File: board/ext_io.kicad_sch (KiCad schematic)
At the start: 34 parts, among them J10 CAN_2, J6 AIN, J7 CAN_1, J8 DIO1, J9 DIO0, SW16 Term, SW17 Term, U13 25LCxxx, U14 MCP2515-xP, U15 MCP3204, U16 MCP2562-E-P, U17 MCP2515-xP, U18 MCP23S17_SP, U19 MCP2562-E-P, Y2 16MHz, Y3 16MHz

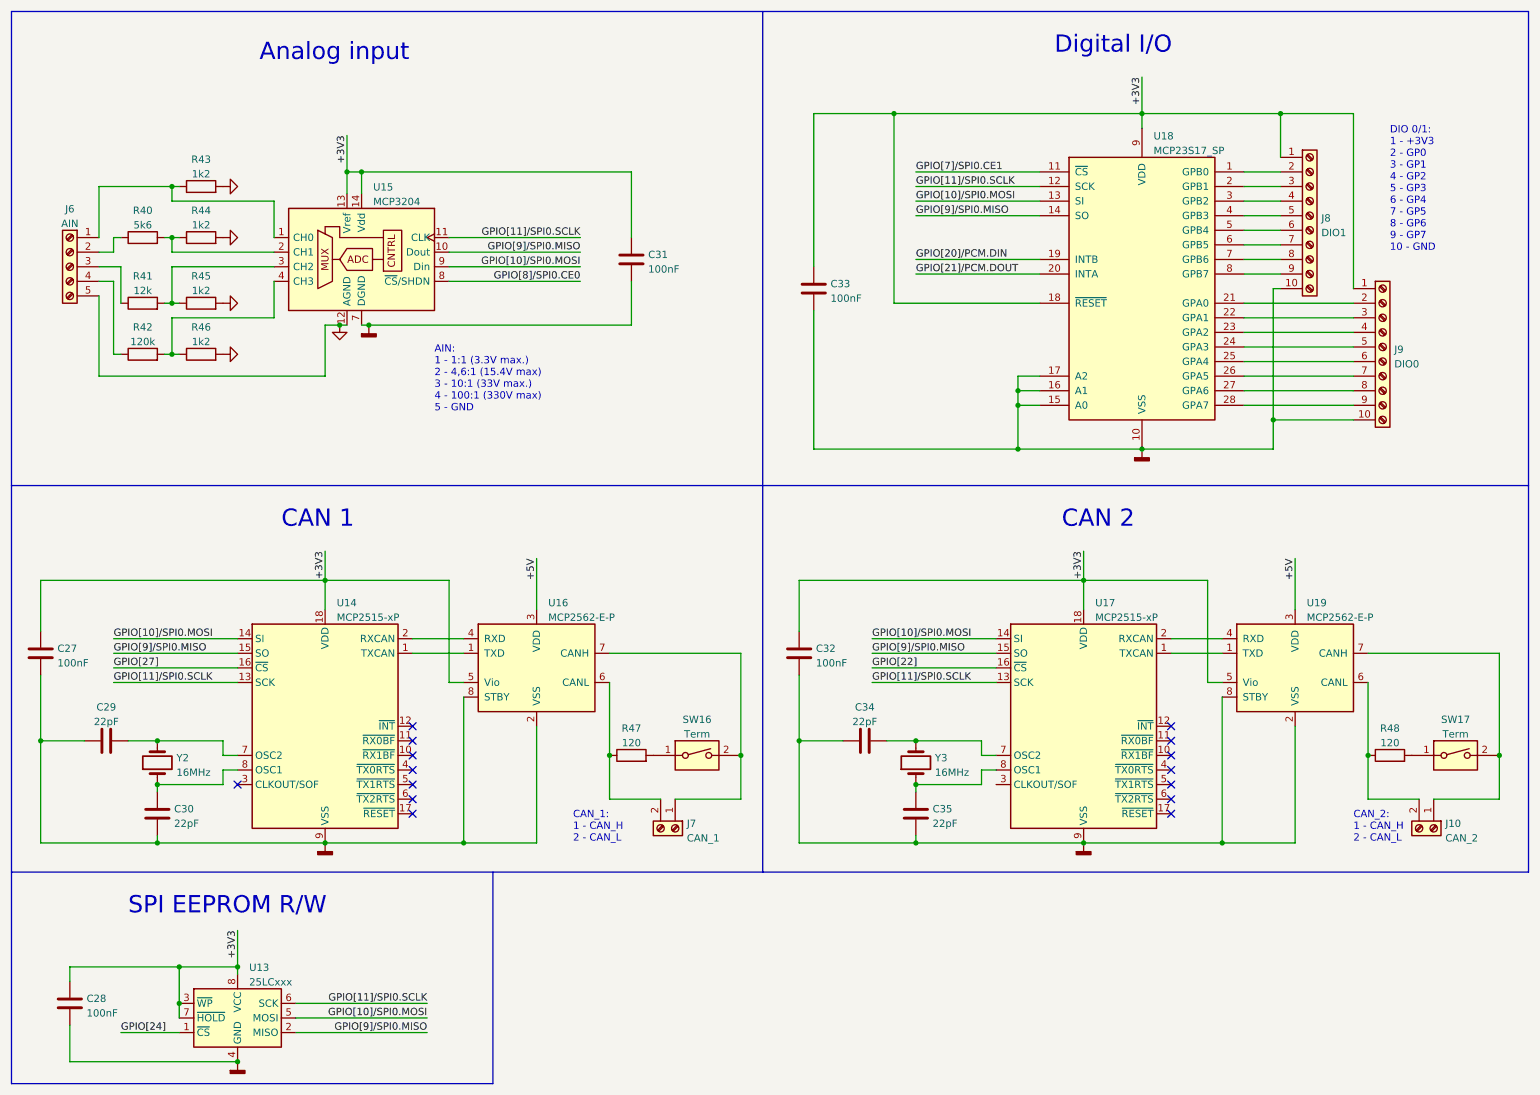
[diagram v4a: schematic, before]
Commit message: Add missing footprints.
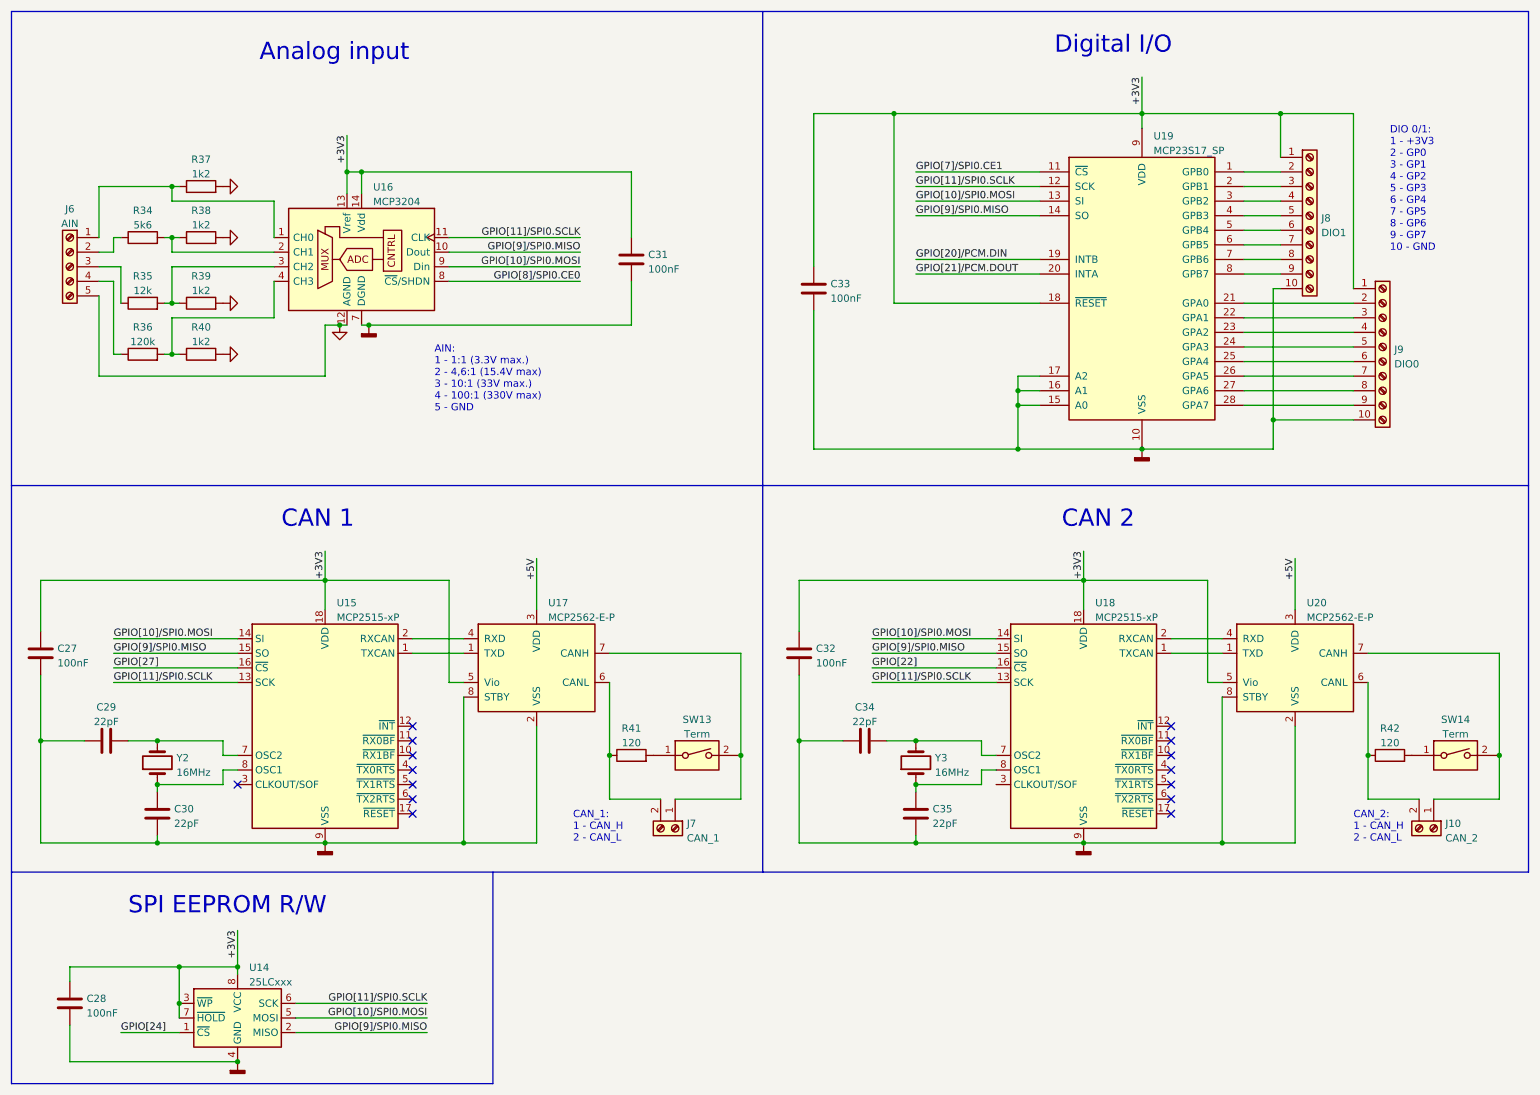
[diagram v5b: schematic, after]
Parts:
- C27, C28, C31, C32, C33, C34, C35: footprint (none) -> Capacitor_THT:C_Disc_D5.0mm_W2.5mm_P5.00mm
- C29, C30: footprint (none) -> Capacitor_THT:C_Radial_D6.3mm_H5.0mm_P2.50mm
- J10, J7: footprint (none) -> TerminalBlock_TE-Connectivity:TerminalBlock_TE_282834-2_1x02_P2.54mm_Horizontal
- J6: footprint (none) -> TerminalBlock_TE-Connectivity:TerminalBlock_TE_282834-5_1x05_P2.54mm_Horizontal
- J8, J9: footprint (none) -> TerminalBlock_TE-Connectivity:TerminalBlock_TE_1-282834-0_1x10_P2.54mm_Horizontal
- R34: renamed from R40; footprint (none) -> Resistor_THT:R_Axial_DIN0516_L15.5mm_D5.0mm_P7.62mm_Vertical
- R35: renamed from R41; footprint (none) -> Resistor_THT:R_Axial_DIN0516_L15.5mm_D5.0mm_P7.62mm_Vertical
- R36: renamed from R42; footprint (none) -> Resistor_THT:R_Axial_DIN0516_L15.5mm_D5.0mm_P7.62mm_Vertical
- R37: renamed from R43; footprint (none) -> Resistor_THT:R_Axial_DIN0516_L15.5mm_D5.0mm_P7.62mm_Vertical
- R38: renamed from R44; footprint (none) -> Resistor_THT:R_Axial_DIN0516_L15.5mm_D5.0mm_P7.62mm_Vertical
- R39: renamed from R45; footprint (none) -> Resistor_THT:R_Axial_DIN0516_L15.5mm_D5.0mm_P7.62mm_Vertical
- R40: renamed from R46; footprint (none) -> Resistor_THT:R_Axial_DIN0516_L15.5mm_D5.0mm_P7.62mm_Vertical
- R41: renamed from R47; footprint (none) -> Resistor_THT:R_Axial_DIN0516_L15.5mm_D5.0mm_P7.62mm_Vertical
- R42: renamed from R48; footprint (none) -> Resistor_THT:R_Axial_DIN0516_L15.5mm_D5.0mm_P7.62mm_Vertical
- SW13: renamed from SW16; footprint (none) -> Button_Switch_THT:SW_DIP_SPSTx01_Slide_6.7x4.1mm_W7.62mm_P2.54mm_LowProfile
- SW14: renamed from SW17; footprint (none) -> Button_Switch_THT:SW_DIP_SPSTx01_Slide_6.7x4.1mm_W7.62mm_P2.54mm_LowProfile
- U16: renamed from U15; footprint (none) -> Package_DIP:DIP-12_W7.62mm_Socket_LongPads
- Y2, Y3: footprint (none) -> Crystal:Crystal_HC49-U_Vertical
- renumbered U13 to U14, U14 to U15, U16 to U17, U17 to U18, U18 to U19, U19 to U20

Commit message: Change net descriptors.
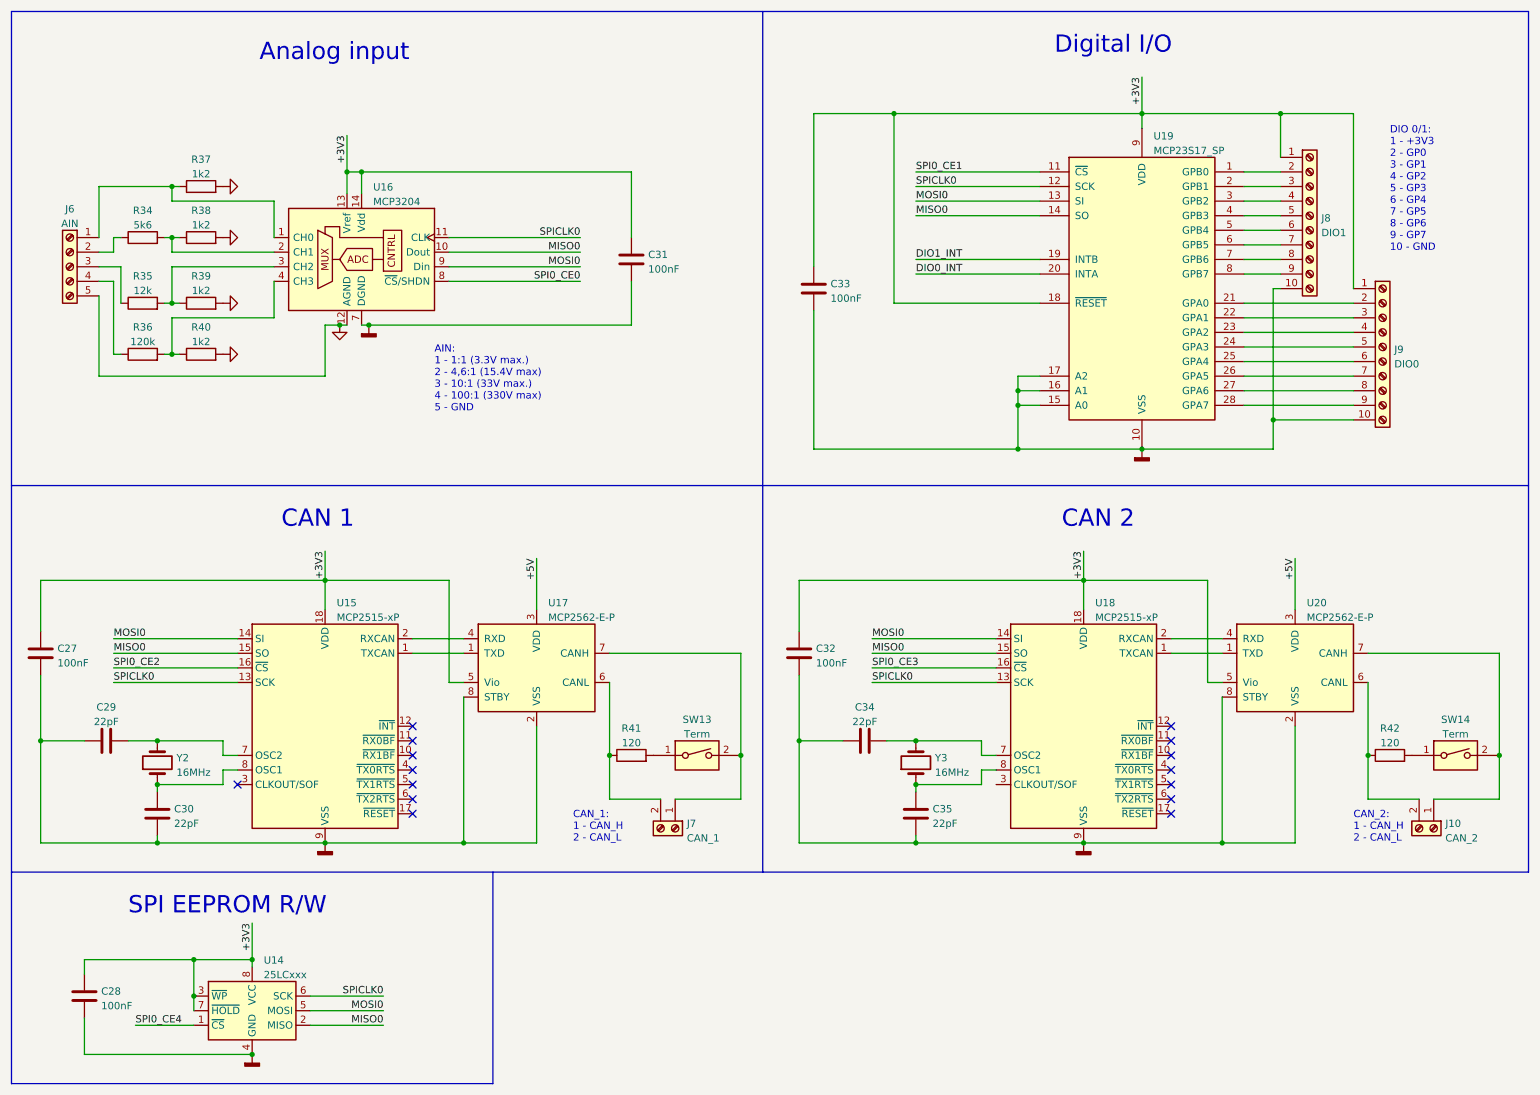
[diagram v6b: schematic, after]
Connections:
- net GPIO[10]/SPI0.MOSI renamed MOSI0
- net GPIO[11]/SPI0.SCLK renamed SPICLK0
- net GPIO[20]/PCM.DIN renamed DIO1_INT
- net GPIO[21]/PCM.DOUT renamed DIO0_INT
- net GPIO[22] renamed SPI0_CE3
- net GPIO[24] renamed SPI0_CE4
- net GPIO[27] renamed SPI0_CE2
- net GPIO[7]/SPI0.CE1 renamed SPI0_CE1
- net GPIO[8]/SPI0.CE0 renamed SPI0_CE0
- net GPIO[9]/SPI0.MISO renamed MISO0
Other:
- moved on the sheet: C28, U14

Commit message: Make it a multiboard project.
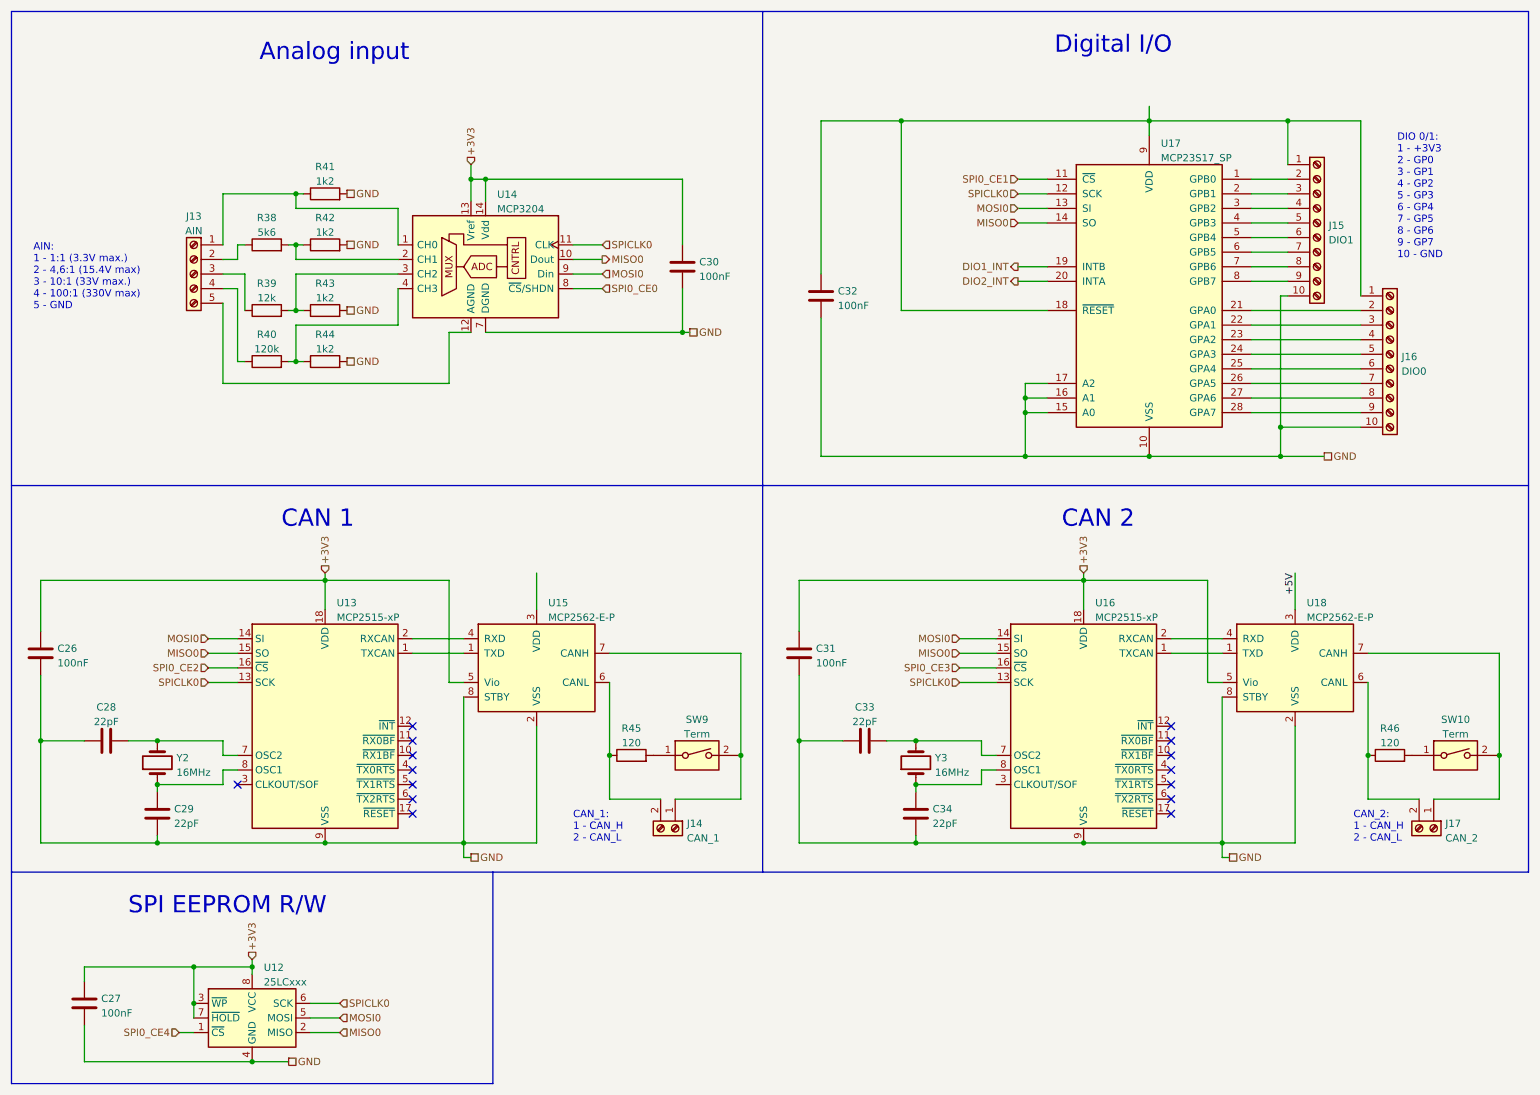
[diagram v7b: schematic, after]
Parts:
- renumbered C27 to C26, C28 to C27, C29 to C28, C30 to C29, C31 to C30, C32 to C31, C33 to C32, C34 to C33, C35 to C34, J6 to J13, J7 to J14, J8 to J15, J9 to J16, J10 to J17, R34 to R38, R35 to R39, R36 to R40, R37 to R41, R38 to R42, R39 to R43, R40 to R44, R41 to R45, R42 to R46, SW14 to SW10, SW13 to SW9, U14 to U12, U15 to U13, U16 to U14, U17 to U15, U18 to U16, U19 to U17, U20 to U18
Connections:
- net GNDD is gone; now on net GND: C26.1, C27.2, C28.1, C29.2, C30.1, C31.1, C32.2, C33.1, C34.2, J15.10 (Pin_10), J16.10 (Pin_10), U12.4 (GND), U13.9 (VSS), U14.7 (DGND), U15.2 (VSS), U15.8 (STBY), U16.9 (VSS), U17.10 (VSS), U17.15 (A0), U17.16 (A1), U17.17 (A2), U18.2 (VSS), U18.8 (STBY)
- net +3V3: no longer C32.1, J15.1 (Pin_1), J16.1 (Pin_1), U17.18 (~{RESET}), U17.9 (VDD)
- net +5V: no longer U15.3 (VDD)
- net DIO0_INT renamed DIO2_INT
- net GNDA renamed GND
- net GND: no longer J13.5 (Pin_5), U14.12 (AGND)
- new net: C32.1, J15.1 (Pin_1), J16.1 (Pin_1), U17.18 (~{RESET}), U17.9 (VDD)
- new net: J13.5 (Pin_5), U14.12 (AGND)
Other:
- moved on the sheet: C27, C30, C32, J13, J15, J16, R38, R39, R40, R41, R42, R43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
